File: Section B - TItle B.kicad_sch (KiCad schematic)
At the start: 0 parts

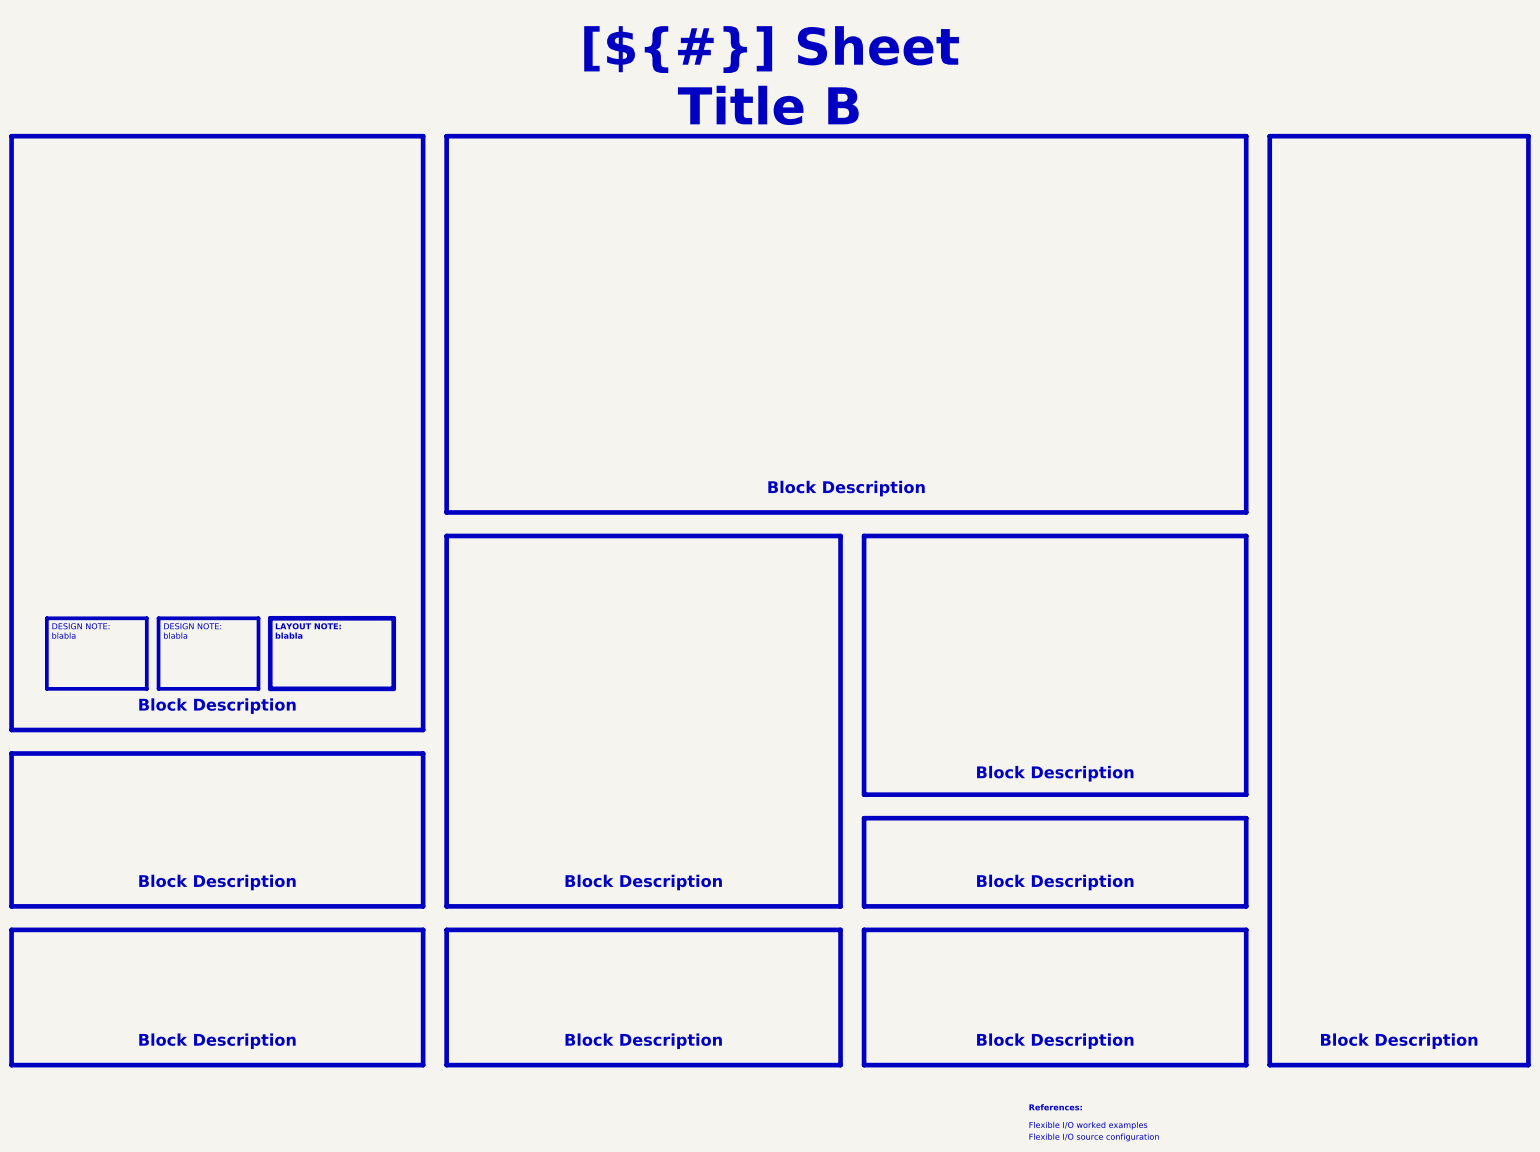
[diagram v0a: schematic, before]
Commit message: [Schematics] Merging changes from the initial project to the Template
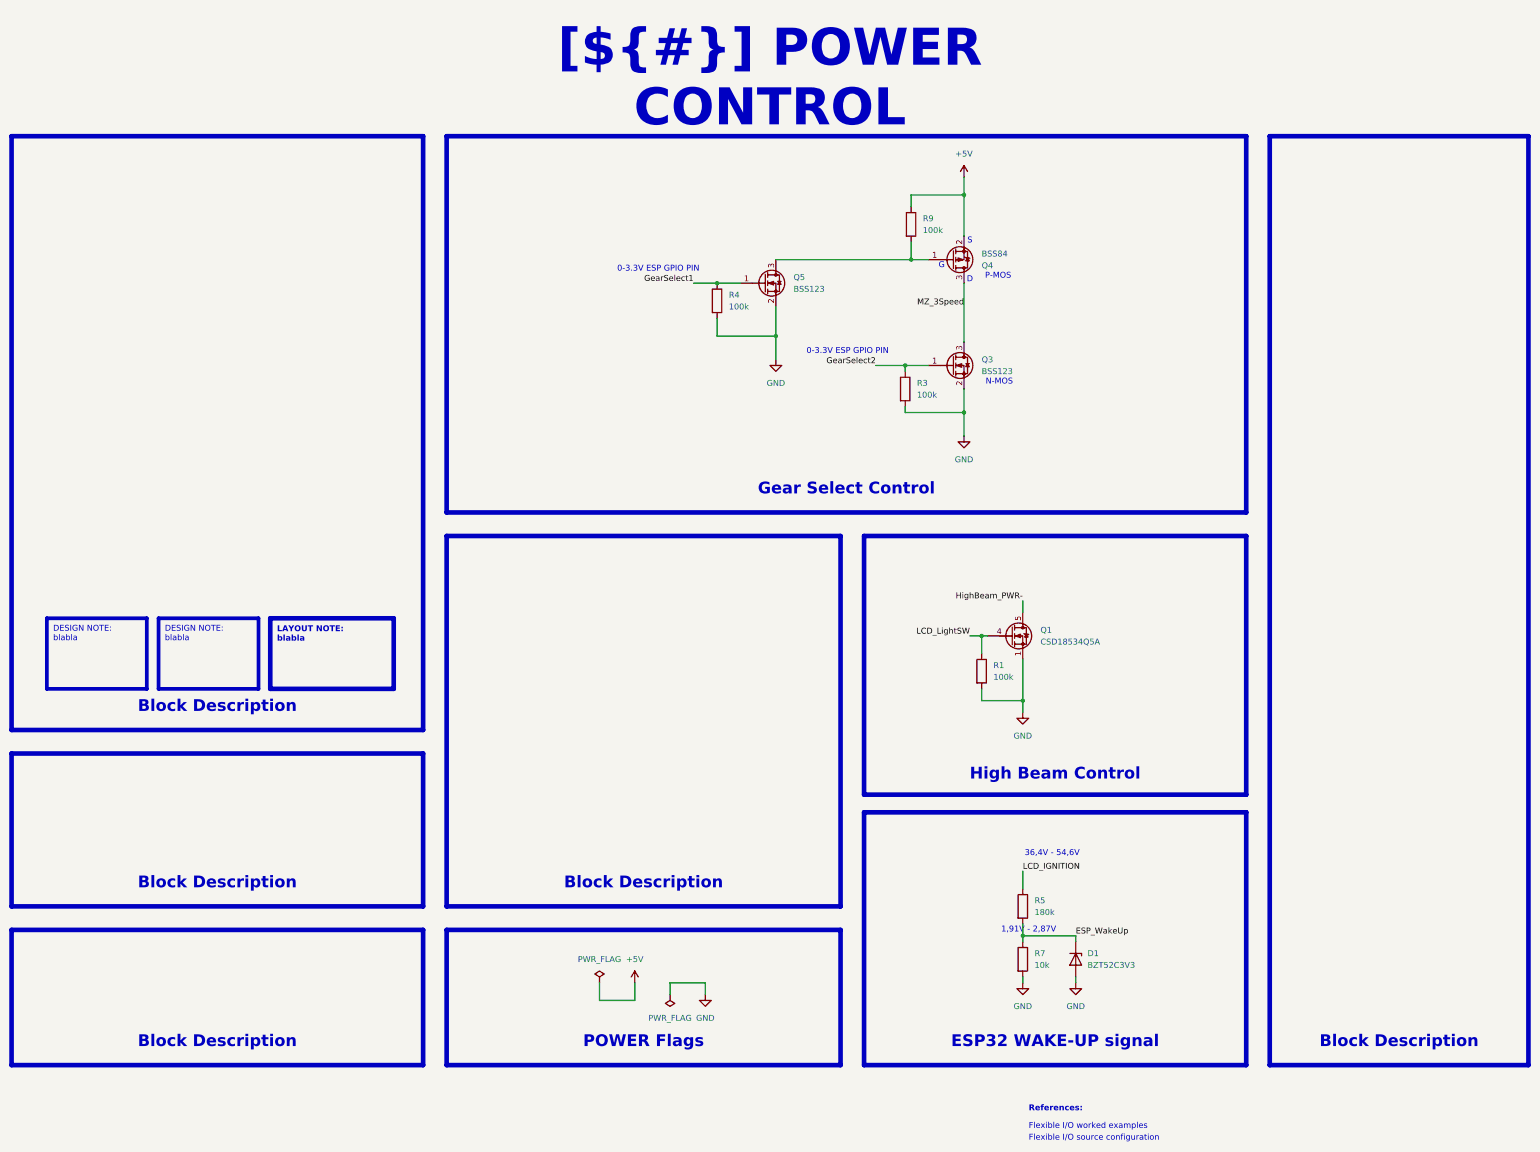
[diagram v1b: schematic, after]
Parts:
- added D1: BZT52C3V3, Diode_SMD:D_SOD-123F, symbol Device:D_Zener
- added Q1: CSD18534Q5A, Package_TO_SOT_SMD:TDSON-8-1, symbol Transistor_FET:CSD18534Q5A
- added Q3, Q5: BSS123, Package_TO_SOT_SMD:SOT-23, symbol Transistor_FET:BSS123
- added Q4: BSS84, Package_TO_SOT_SMD:SOT-23, symbol Transistor_FET:BSS84
- added R1, R3, R4, R9: 100k, Resistor_SMD:R_0603_1608Metric_Pad0.98x0.95mm_HandSolder, symbol Device:R
- added R5: 180k, Resistor_SMD:R_0603_1608Metric_Pad0.98x0.95mm_HandSolder, symbol Device:R
- added R7: 10k, Resistor_SMD:R_0603_1608Metric_Pad0.98x0.95mm_HandSolder, symbol Device:R
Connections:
- new net: Q4.1 (G), Q5.3 (D), R9.2
- new net +5V: Q4.2 (S), R9.1
- new net ESP_WakeUp: D1.1 (K), R5.2, R7.1
- new net GND: D1.2 (A), Q1.1 (S), Q1.2 (S), Q1.3 (S), Q3.2 (S), Q5.2 (S), R1.2, R3.2, R4.2, R7.2
- new net GearSelect1: Q5.1 (G), R4.1
- new net GearSelect2: Q3.1 (G), R3.1
- new net HighBeam_PWR-: Q1.5 (D)
- new net LCD_IGNITION: R5.1
- new net LCD_LightSW: Q1.4 (G), R1.1
- new net MZ_3Speed: Q3.3 (D), Q4.3 (D)
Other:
- note added: "0-3.3V ESP GPIO PIN"
- note added: "1,91V - 2,87V"
- note added: "36,4V - 54,6V"
- note added: "D"
- note added: "G"
- note added: "N-MOS"
- note added: "P-MOS"
- note added: "S"
- title: Sheet Title B -> POWER CONTROL
